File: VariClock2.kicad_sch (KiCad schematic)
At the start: 30 parts, among them Q25 2N3904, Q26 2N3906, Q27 2N3904

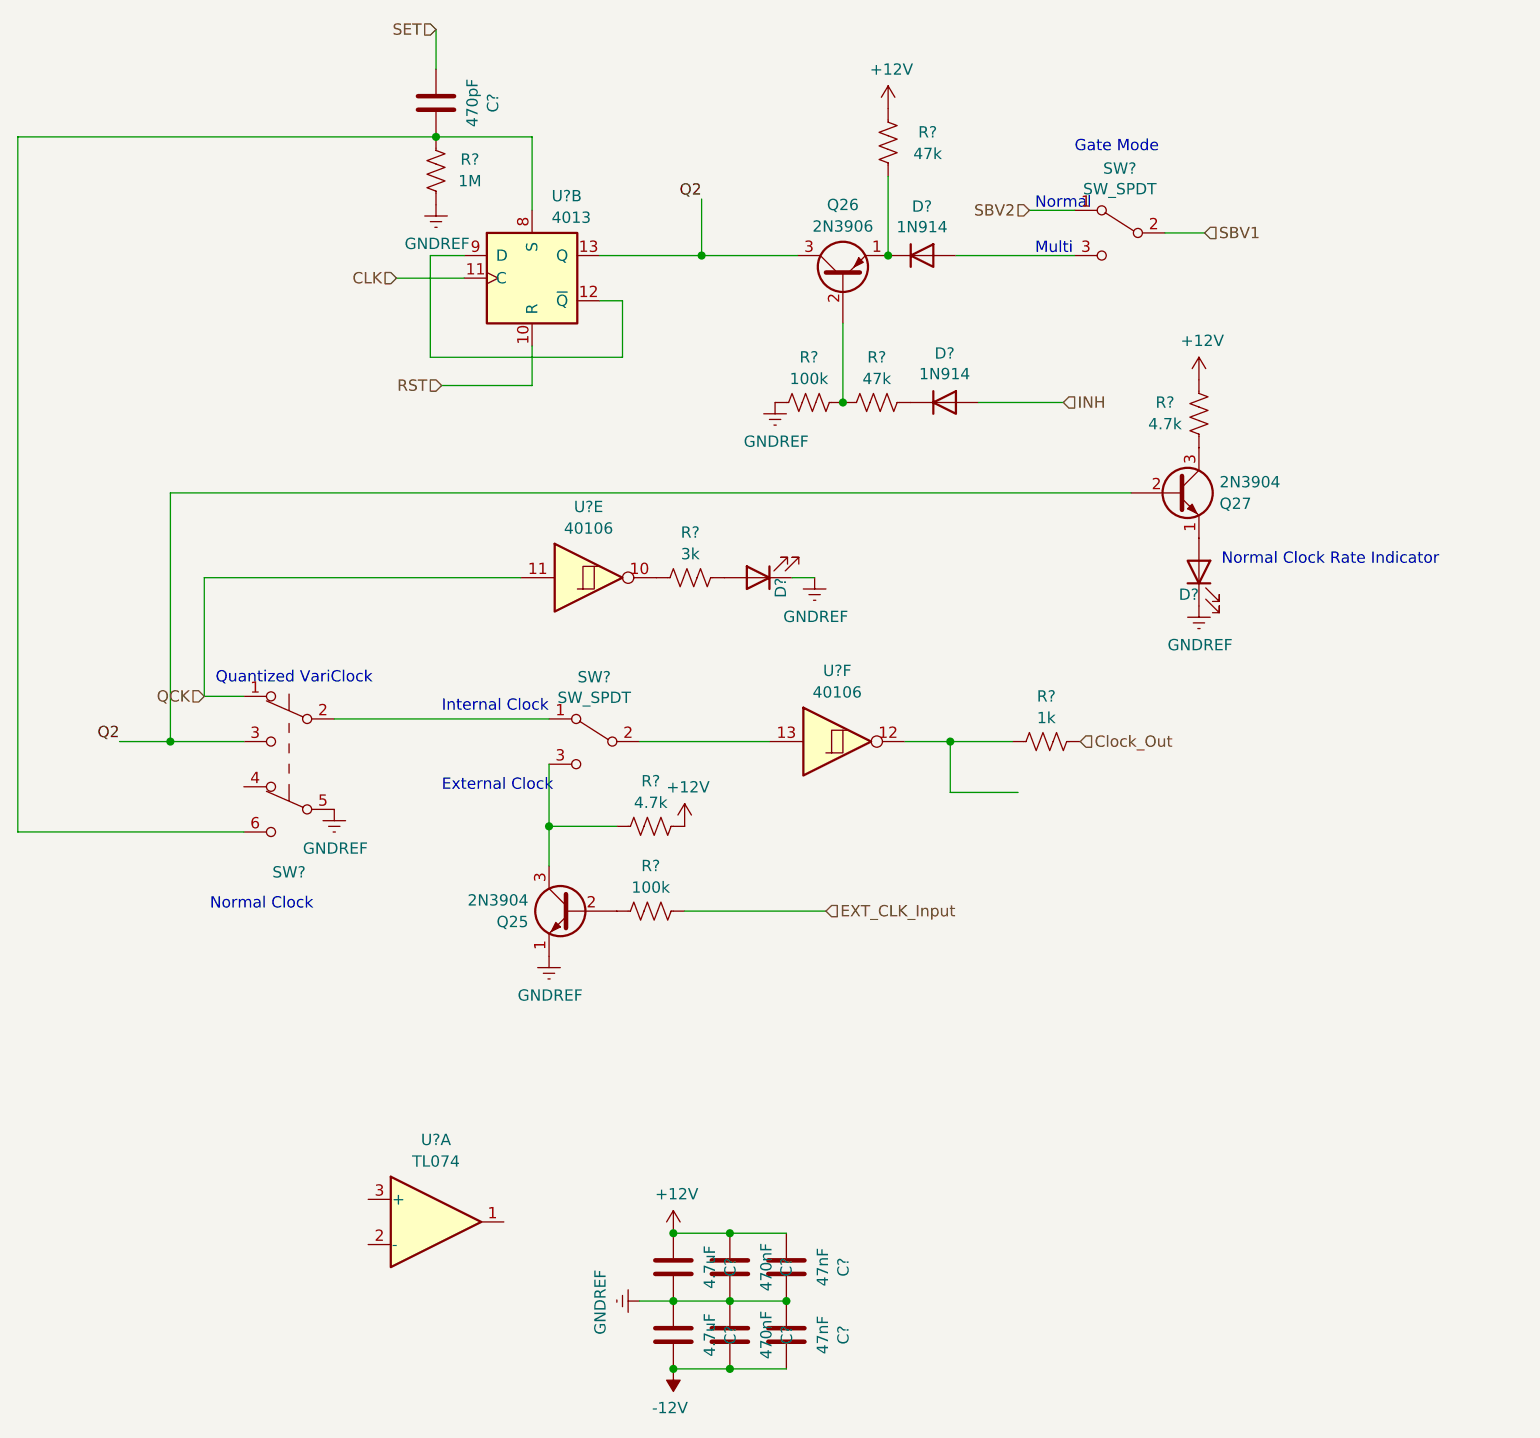
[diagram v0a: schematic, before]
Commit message: created pcb file, placed parts
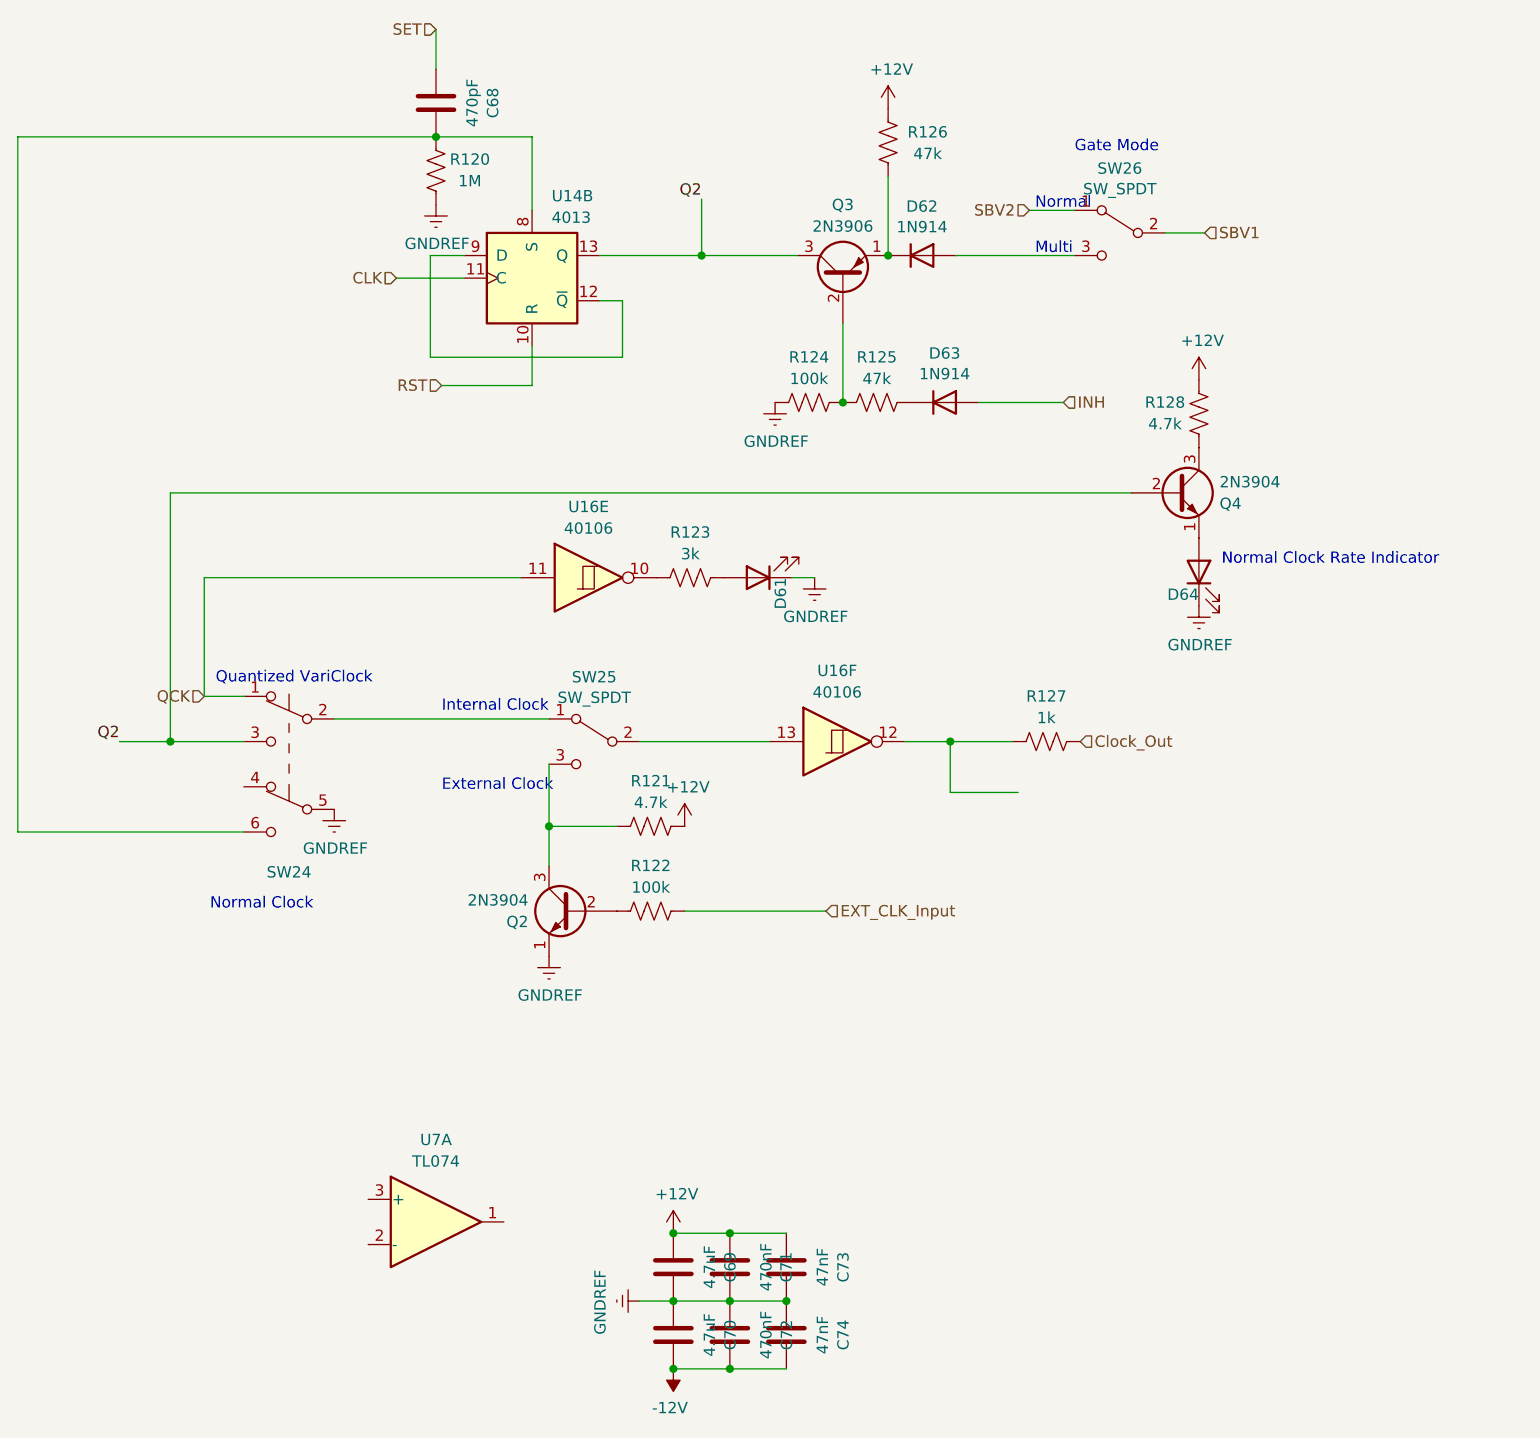
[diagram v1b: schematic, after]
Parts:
- gave numbers to parts that had none: 26
- renumbered Q25 to Q2, Q26 to Q3, Q27 to Q4

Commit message: routing and placing
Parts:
- D61, D64: footprint LED_SMD:LED_0805_2012Metric -> LED_THT:LED_D5.0mm
- Q2, Q4: value 2N3904 -> MMBT3904-7-F; footprint Package_TO_SOT_THT:TO-92_Inline -> Package_TO_SOT_SMD:SOT-23-3
- Q3: value 2N3906 -> MMBT3906; footprint Package_TO_SOT_THT:TO-92_Inline -> Package_TO_SOT_SMD:SOT-23-3
- renumbered U14 to U4
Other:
- note added: "Quantized Clock Rate Indicator"
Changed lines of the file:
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@@
+    (effects (font (size 1.27 1.27)) (justify left bottom))
+  )
+  (text "Quantized Clock Rate Indicator" (at 151.13 92.71 0)
     (effects (font (size 1.27 1.27)) (justify left bottom))
   )
@@
       (effects (font (size 1.27 1.27)) (justify left))
     )
-    (property "Value" "2N3904" (at 129.7686 134.0429 0)
+    (property "Value" "MMBT3904-7-F" (at 129.7686 134.0429 0)
       (effects (font (size 1.27 1.27)) (justify left))
     )
-    (property "Footprint" "Package_TO_SOT_THT:TO-92_Inline" (at 129.54 137.16 0)
+    (property "Footprint" "Package_TO_SOT_SMD:SOT-23-3" (at 129.54 137.16 0)
       (effects (font (size 1.27 1.27) italic) (justify left) hide)
     )
@@
       (effects (font (size 1.27 1.27)))
     )
-    (property "Value" "2N3906" (at 165.1 58.3255 90)
-      (effects (font (size 1.27 1.27)))
-    )
-    (property "Footprint" "Package_TO_SOT_THT:TO-92_Inline" (at 167.005 59.055 0)
+    (property "Value" "MMBT3906" (at 165.1 58.3255 90)
+      (effects (font (size 1.27 1.27)))
+    )
+    (property "Footprint" "Package_TO_SOT_SMD:SOT-23-3" (at 167.005 59.055 0)
       (effects (font (size 1.27 1.27) italic) (justify left) hide)
     )
@@
       (effects (font (size 1.27 1.27)) (justify left))
     )
-    (property "Value" "2N3904" (at 207.4164 87.0529 0)
+    (property "Value" "MMBT3904-7-F" (at 207.4164 87.0529 0)
       (effects (font (size 1.27 1.27)) (justify left))
     )
-    (property "Footprint" "Package_TO_SOT_THT:TO-92_Inline" (at 207.645 90.17 0)
+    (property "Footprint" "Package_TO_SOT_SMD:SOT-23-3" (at 207.645 90.17 0)
       (effects (font (size 1.27 1.27) italic) (justify left) hide)
     )
@@
   (symbol (lib_id "4xxx:4013") (at 130.175 64.135 0) (unit 2)
     (in_bom yes) (on_board yes) (dnp no) (fields_autoplaced)
-    (property "Reference" "U14" (at 132.3691 54.9107 0)
+    (property "Reference" "U4" (at 132.3691 54.61 0)
       (effects (font (size 1.27 1.27)) (justify left))
     )
-    (property "Value" "4013" (at 132.3691 57.3349 0)
+    (property "Value" "4013" (at 132.3691 57.15 0)
       (effects (font (size 1.27 1.27)) (justify left))
     )
@@
       (project "SoundLab16StepSequencer"
         (path "/0a1377c9-61ff-44bc-b9df-99baf54c0c4b/ba12edcc-425a-4e43-95e4-b634dcdc7d8b"
-          (reference "U14") (unit 2)
+          (reference "U4") (unit 2)
         )
       )
@@
       (effects (font (size 1.27 1.27)) (justify left) hide)
     )
-    (property "Footprint" "LED_SMD:LED_0805_2012Metric" (at 155.575 97.79 0)
+    (property "Footprint" "LED_THT:LED_D5.0mm" (at 155.575 97.79 0)
       (effects (font (size 1.27 1.27)) hide)
     )
@@
       (effects (font (size 1.27 1.27)) (justify left) hide)
     )
-    (property "Footprint" "LED_SMD:LED_0805_2012Metric" (at 205.105 97.155 0)
-      (effects (font (size 1.27 1.27)) hide)
-    )
+    (property "Footprint" "LED_THT:LED_D5.0mm" (at 205.105 97.155 0)
+      (effects (font (size 1.27 1.27)) hide)
+    )

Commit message: routed 100%
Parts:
- removed C69, C70: 4.7uF, Capacitor_SMD:C_0805_2012Metric, symbol Device:C
- removed C71, C72: 470nF, Capacitor_SMD:C_0805_2012Metric, symbol Device:C
- removed C73, C74: 47nF, Capacitor_SMD:C_0603_1608Metric, symbol Device:C
- added C50, C52: 470nF, Capacitor_SMD:C_0805_2012Metric, symbol Device:C
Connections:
- net +12V: now also C52.1
- net -12V: now also C50.2
- net GNDREF: now also C50.1, C52.2
